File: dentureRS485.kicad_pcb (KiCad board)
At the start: 2 copper layers, 54 x 54 mm, 28 parts, among them J1 Conn_01x04, J2 Conn_01x08, J3 free_holes, J4 Conn_01x08, J5 Conn_01x02, U1 SP3485EN

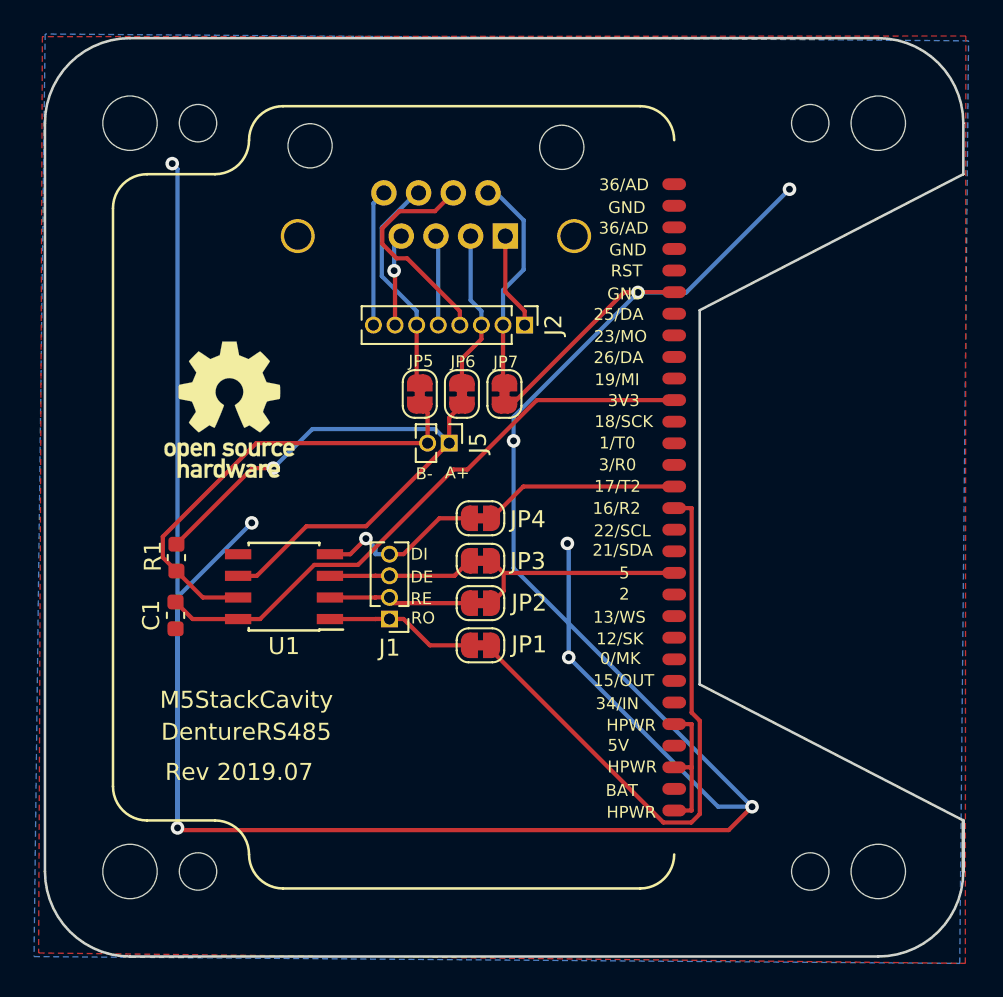
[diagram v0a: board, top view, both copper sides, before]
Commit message: Change position of lan jack on pcb
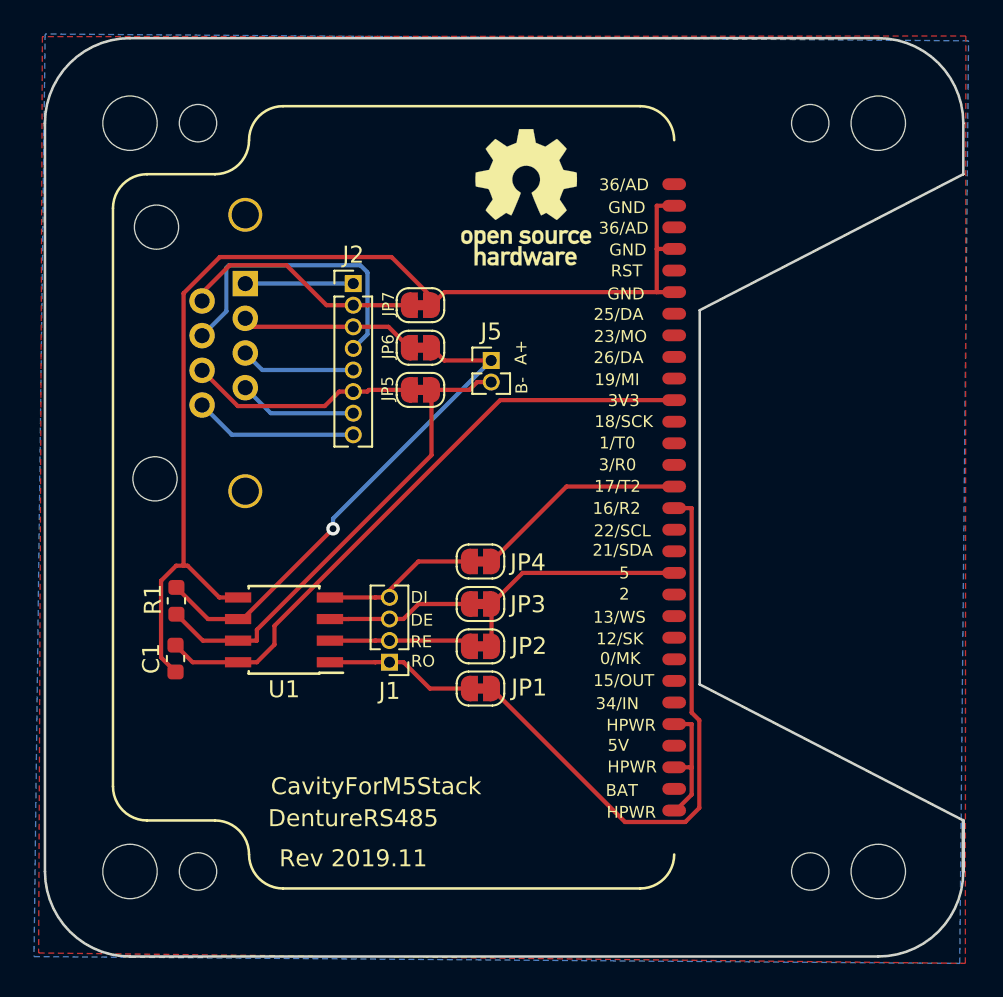
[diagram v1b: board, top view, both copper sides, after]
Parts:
- moved OSHWREF2 21.5 mm to (126.3, 57.4)
- moved J4 15.5 mm to (109.8, 62.4), turned to 90 degrees
- moved J2 10.4 mm to (116.1, 62.4), turned to 0 degrees
- moved JP7 7.19 mm to (120.1, 63.7), turned to 0 degrees
- moved J5 5.45 mm to (124.2, 67.0), turned to 0 degrees
- moved JP6 3.65 mm to (120.1, 66.2), turned to 0 degrees
- moved J1 2.54 mm to (118.3, 84.7)
- moved JP1 2.54 mm to (123.6, 86.2)
- moved JP3 2.54 mm to (123.6, 81.3)
- moved JP4 2.54 mm to (123.6, 78.8)
- moved R1 2.54 mm to (105.7, 81.1)
- moved U1 2.54 mm to (112.1, 82.8)
- moved C1 2.54 mm to (105.7, 84.5)
- moved JP2 2.54 mm to (123.6, 83.8)
- moved JP5 0.24 mm to (120.1, 68.7), turned to 0 degrees
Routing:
- net GND: track 177.7 -> 65.9 mm, vias 9 -> 0
- net /A+: track 37.4 -> 29.7 mm
- net Net-(J2-Pad4): track 13.0 -> 17.9 mm
- net +3V3: track 35.1 -> 36.8 mm
- net Net-(J2-Pad8): track 8.03 -> 9.61 mm
- net Net-(J2-Pad7): track 5.43 -> 6.97 mm, vias 1 -> 0
- net /16: track 36.2 -> 34.7 mm
- net Net-(J2-Pad5): track 5.29 -> 6.76 mm
- net Net-(J2-Pad2): track 12.9 -> 14.3 mm
- net /B-: track 26.9 -> 28.1 mm
- net /17: track 11.5 -> 12.6 mm
- net Net-(J2-Pad3): track 9.37 -> 10.4 mm
- net /5: track 13.1 -> 14.0 mm
- net Net-(J2-Pad1): track 5.70 -> 6.35 mm
- net Net-(J1-Pad4): track 10.0 -> 9.49 mm, vias 1 -> 0
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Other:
- board text added: "CavityForM5Stack"
- board text added: "Rev 2019.11"
- board text removed: "M5StackCavity"
- board text removed: "Rev 2019.07"

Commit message: Add via for GND
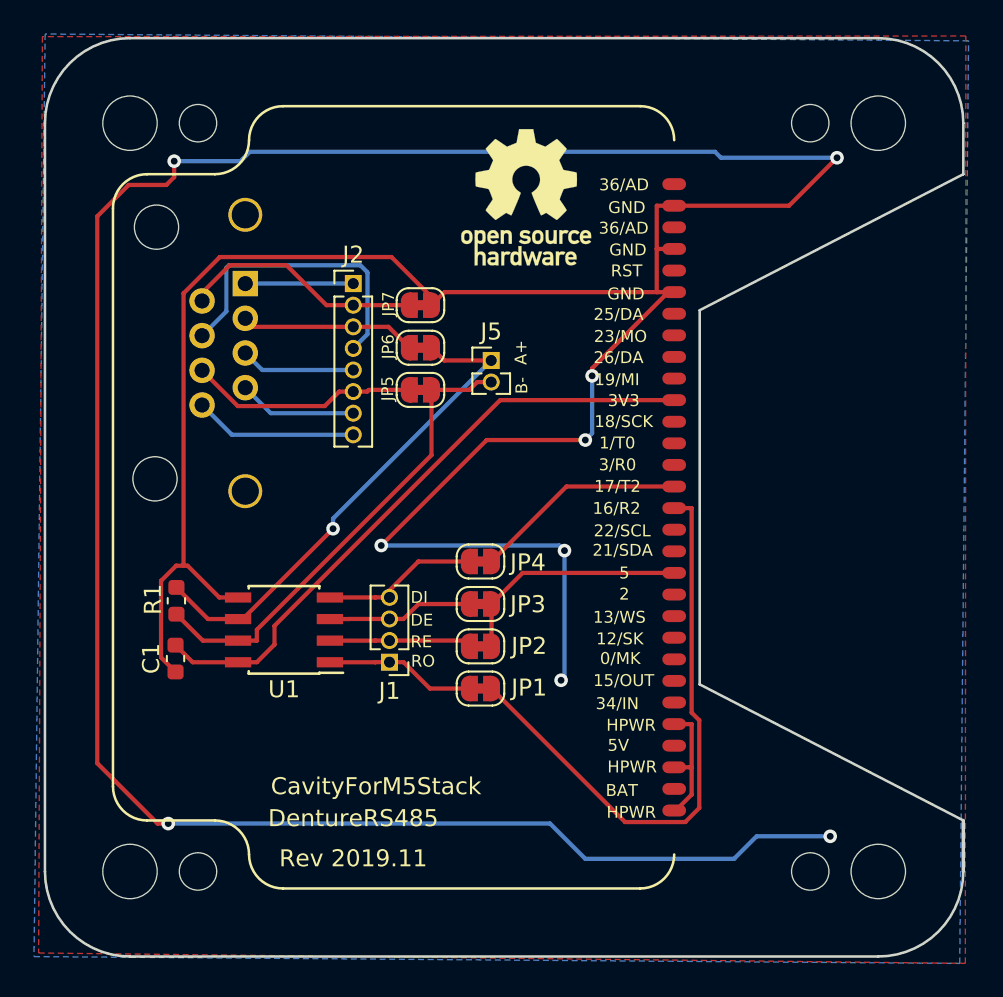
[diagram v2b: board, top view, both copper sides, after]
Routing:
- net GND: track 65.9 -> 244.8 mm, vias 0 -> 9
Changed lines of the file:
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@@
-(kicad_pcb (version 20171130) (host pcbnew "(5.1.4-0-10_14)")
+(kicad_pcb (version 20171130) (host pcbnew 5.1.4-e60b266~84~ubuntu18.04.1)
   (general
     (thickness 1.6)
     (drawings 60)
-    (tracks 123)
+    (tracks 163)
     (zones 0)
     (modules 28)
@@
   (segment (start 133.9747 60.395) (end 133.9747 57.855) (width 0.25) (layer F.Cu) (net 1))
   (segment (start 135 60.395) (end 133.9747 60.395) (width 0.25) (layer F.Cu) (net 1))
+  (via (at 144.5738 55.0332) (size 0.8) (drill 0.4) (layers F.Cu B.Cu) (net 1))
+  (segment (start 135 57.855) (end 141.752 57.855) (width 0.25) (layer F.Cu) (net 1))
+  (segment (start 141.752 57.855) (end 144.5738 55.0332) (width 0.25) (layer F.Cu) (net 1))
+  (segment (start 144.5738 55.0332) (end 137.7488 55.0332) (width 0.25) (layer B.Cu) (net 1))
+  (segment (start 137.7488 55.0332) (end 137.3988 54.6832) (width 0.25) (layer B.Cu) (net 1))
+  (segment (start 137.3988 54.6832) (end 110.0488 54.6832) (width 0.25) (layer B.Cu) (net 1))
+  (via (at 105.5988 55.2332) (size 0.8) (drill 0.4) (layers F.Cu B.Cu) (net 1))
+  (segment (start 110.0488 54.6832) (end 109.4988 55.2332) (width 0.25) (layer B.Cu) (net 1))
+  (segment (start 109.4988 55.2332) (end 105.5988 55.2332) (width 0.25) (layer B.Cu) (net 1))
+  (segment (start 105.5988 56.169002) (end 105.134602 56.6332) (width 0.25) (layer F.Cu) (net 1))
+  (segment (start 105.5988 55.2332) (end 105.5988 56.169002) (width 0.25) (layer F.Cu) (net 1))
+  (segment (start 105.134602 56.6332) (end 102.9238 56.6332) (width 0.25) (layer F.Cu) (net 1))
+  (segment (start 101.074999 58.482001) (end 101.074999 90.634399) (width 0.25) (layer F.Cu) (net 1))
+  (segment (start 102.9238 56.6332) (end 101.074999 58.482001) (width 0.25) (layer F.Cu) (net 1))
+  (via (at 105.2488 94.1832) (size 0.8) (drill 0.4) (layers F.Cu B.Cu) (net 1))
+  (segment (start 101.074999 90.634399) (end 104.6238 94.1832) (width 0.25) (layer F.Cu) (net 1))
+  (segment (start 104.6238 94.1832) (end 105.2488 94.1832) (width 0.25) (layer F.Cu) (net 1))
+  (segment (start 105.2488 94.1832) (end 127.6988 94.1832) (width 0.25) (layer B.Cu) (net 1))
+  (segment (start 127.6988 94.1832) (end 129.7738 96.2582) (width 0.25) (layer B.Cu) (net 1))
+  (segment (start 129.7738 96.2582) (end 138.5238 96.2582) (width 0.25) (layer B.Cu) (net 1))
+  (via (at 144.1738 94.9332) (size 0.8) (drill 0.4) (layers F.Cu B.Cu) (net 1))
+  (segment (start 138.5238 96.2582) (end 139.8488 94.9332) (width 0.25) (layer B.Cu) (net 1))
+  (segment (start 139.8488 94.9332) (end 144.1738 94.9332) (width 0.25) (layer B.Cu) (net 1))
+  (via (at 130.1738 67.8582) (size 0.8) (drill 0.4) (layers F.Cu B.Cu) (net 1))
+  (segment (start 130.1738 67.726592) (end 130.1738 67.8582) (width 0.25) (layer F.Cu) (net 1))
+  (segment (start 130.1738 67.4112) (end 130.1738 67.726592) (width 0.25) (layer F.Cu) (net 1))
+  (segment (start 135 62.935) (end 134.65 62.935) (width 0.25) (layer F.Cu) (net 1))
+  (segment (start 134.65 62.935) (end 130.1738 67.4112) (width 0.25) (layer F.Cu) (net 1))
+  (via (at 129.7738 71.6332) (size 0.8) (drill 0.4) (layers F.Cu B.Cu) (net 1))
+  (segment (start 130.1738 67.8582) (end 130.1738 71.2332) (width 0.25) (layer B.Cu) (net 1))
+  (segment (start 130.1738 71.2332) (end 129.7738 71.6332) (width 0.25) (layer B.Cu) (net 1))
+  (via (at 117.7738 77.8332) (size 0.8) (drill 0.4) (layers F.Cu B.Cu) (net 1))
+  (segment (start 129.7738 71.6332) (end 123.9738 71.6332) (width 0.25) (layer F.Cu) (net 1))
+  (segment (start 123.9738 71.6332) (end 117.7738 77.8332) (width 0.25) (layer F.Cu) (net 1))
+  (via (at 128.5488 78.1332) (size 0.8) (drill 0.4) (layers F.Cu B.Cu) (net 1))
+  (segment (start 117.7738 77.8332) (end 128.2488 77.8332) (width 0.25) (layer B.Cu) (net 1))
+  (segment (start 128.2488 77.8332) (end 128.5488 78.1332) (width 0.25) (layer B.Cu) (net 1))
+  (via (at 128.3488 85.7582) (size 0.8) (drill 0.4) (layers F.Cu B.Cu) (net 1))
+  (segment (start 128.5488 78.1332) (end 128.5488 85.5582) (width 0.25) (layer B.Cu) (net 1))
+  (segment (start 128.5488 85.5582) (end 128.3488 85.7582) (width 0.25) (layer B.Cu) (net 1))
   (segment (start 109.357 84.6979) (end 110.4573 84.6979) (width 0.25) (layer F.Cu) (net 4))
   (segment (start 135 69.285) (end 124.7661 69.285) (width 0.25) (layer F.Cu) (net 4))

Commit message: Save RJ45 connector on my-kicad-footprints
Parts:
- J4: footprint footprints:RJ45_Neltron_Industrial_7810-8P8C -> my-kicad-footprints:LAN_RJ45_Neltron_Industrial_7810-8P8C
